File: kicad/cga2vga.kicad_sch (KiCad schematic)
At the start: 18 parts, among them J1 Conn_02x24_Counter_Clockwise, J2 CGA, J3 VGA, J4 5V, U1 MCP1700-3302E_TO92, U2 SN74LVC245A, U3 SN74LVC245A

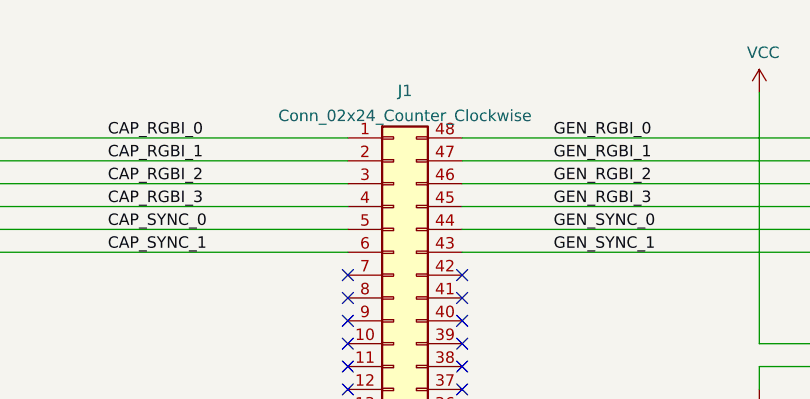
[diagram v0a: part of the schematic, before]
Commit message: Fix power connector marking
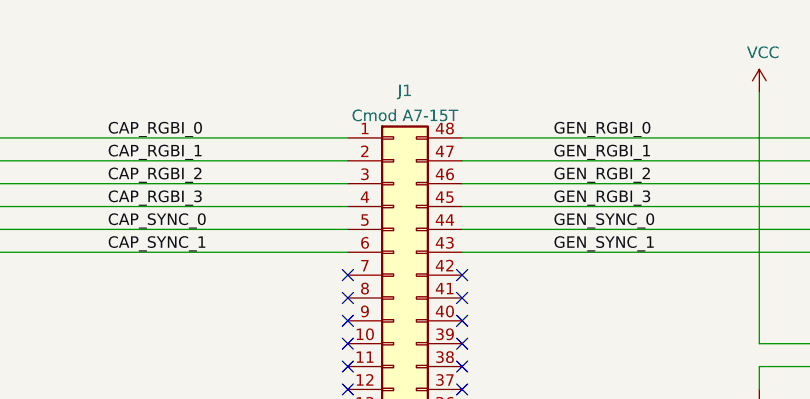
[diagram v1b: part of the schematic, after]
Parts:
- J1: value Conn_02x24_Counter_Clockwise -> Cmod A7-15T
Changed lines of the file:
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@@
     (in_bom yes) (on_board yes) (fields_autoplaced)
     (property "Reference" "J1" (id 0) (at 115.57 44.2935 0))
-    (property "Value" "Conn_02x24_Counter_Clockwise" (id 1) (at 115.57 47.0686 0))
+    (property "Value" "Cmod A7-15T" (id 1) (at 115.57 47.0686 0))
     (property "Footprint" "Package_DIP:DIP-48_W15.24mm_Socket" (id 2) (at 114.3 77.47 0)
       (effects (font (size 1.27 1.27)) hide)
@@
     )
     (path "/4b708762-d3c8-47bb-814c-3cc2597abb3e"
-      (reference "J1") (unit 1) (value "Conn_02x24_Counter_Clockwise") (footprint "Package_DIP:DIP-48_W15.24mm_Socket")
+      (reference "J1") (unit 1) (value "Cmod A7-15T") (footprint "Package_DIP:DIP-48_W15.24mm_Socket")
     )
     (path "/1cf519d2-be13-4b0e-872d-366d38fed7f6"

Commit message: Fix color
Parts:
- added R5, R6: 680, Resistor_THT:R_Axial_DIN0207_L6.3mm_D2.5mm_P7.62mm_Horizontal, symbol Device:R
- R4: value 470 -> 680
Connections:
- net GEN_SYNC_0: now also J1.42 (Pin_42), U3.8 (A6); no longer J1.44 (Pin_44), U3.6 (A4)
- net GEN_SYNC_1: now also J1.41 (Pin_41), U3.9 (A7); no longer J1.43 (Pin_43), U3.7 (A5)
- net VGA_HSYNC: now also U3.12 (B6); no longer U3.14 (B4)
- net VGA_VSYNC: now also U3.11 (B7); no longer U3.13 (B5)
- net at D1.2 (A), R4.2: no longer D2.2 (A), D3.2 (A)
- net GEN_RGBI_0 renamed GEN_RGB0_0
- net GEN_RGBI_1 renamed GEN_RGB0_1
- net GEN_RGBI_2 renamed GEN_RGB0_2
- net GEN_RGBI_3 renamed GEN_RGB1_0
- new net: D2.2 (A), R5.2
- new net: R5.1, U3.14 (B4)
- new net: D3.2 (A), R6.2
- new net: R6.1, U3.13 (B5)
- new net GEN_RGB1_1: J1.44 (Pin_44), U3.6 (A4)
- new net GEN_RGB1_2: J1.43 (Pin_43), U3.7 (A5)
- no-connect marks 48 -> 42
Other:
- moved on the sheet: D1, D2, D3, R1, R2, R3, R4

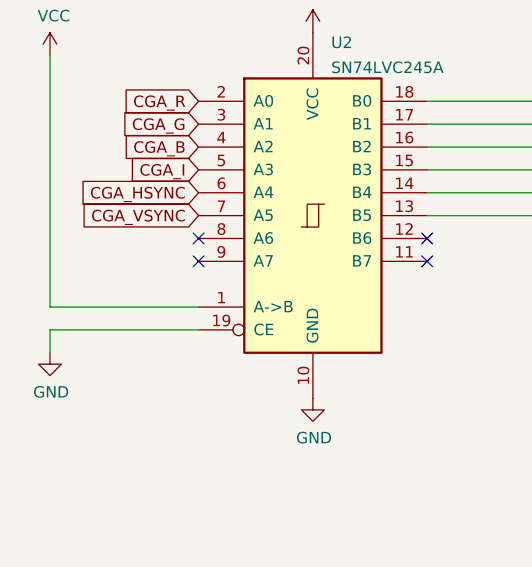
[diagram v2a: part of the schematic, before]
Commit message: Ground unused inputs
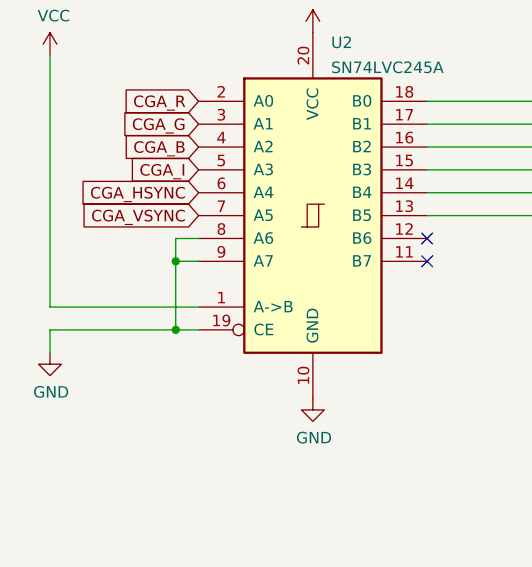
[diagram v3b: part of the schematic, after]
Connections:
- net GND: now also U2.8 (A6), U2.9 (A7)
- no-connect marks 42 -> 40
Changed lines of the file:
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@@
   (junction (at 243.84 57.15) (diameter 0) (color 0 0 0 0)
   )
+  (junction (at 40.64 67.31) (diameter 0) (color 0 0 0 0)
+  )
   (junction (at 86.36 189.23) (diameter 0) (color 0 0 0 0)
+  )
+  (junction (at 40.64 74.93) (diameter 0) (color 0 0 0 0)
   )
   (junction (at 73.66 181.61) (diameter 0) (color 0 0 0 0)
@@
   (no_connect (at 121.92 69.85))
   (no_connect (at 228.6 129.54))
-  (no_connect (at 43.18 64.77))
-  (no_connect (at 43.18 67.31))
   (no_connect (at 228.6 127))
   (no_connect (at 228.6 114.3))
@@
     (stroke (width 0) (type default) (color 0 0 0 0))
   )
+  (wire (pts (xy 40.64 64.77) (xy 40.64 67.31))
+    (stroke (width 0) (type default) (color 0 0 0 0))
+  )
+  (wire (pts (xy 40.64 74.93) (xy 43.18 74.93))
+    (stroke (width 0) (type default) (color 0 0 0 0))
+  )
   (wire (pts (xy 243.84 77.47) (xy 243.84 88.9))
     (stroke (width 0) (type default) (color 0 0 0 0))
@@
     (stroke (width 0) (type default) (color 0 0 0 0))
   )
+  (wire (pts (xy 40.64 67.31) (xy 43.18 67.31))
+    (stroke (width 0) (type default) (color 0 0 0 0))
+  )
   (wire (pts (xy 172.72 123.19) (xy 187.96 123.19))
     (stroke (width 0) (type default) (color 0 0 0 0))
@@
     (stroke (width 0) (type default) (color 0 0 0 0))
   )
+  (wire (pts (xy 40.64 67.31) (xy 40.64 74.93))
+    (stroke (width 0) (type default) (color 0 0 0 0))
+  )
   (wire (pts (xy 191.77 62.23) (xy 210.82 62.23))
     (stroke (width 0) (type default) (color 0 0 0 0))
@@
     (stroke (width 0) (type default) (color 0 0 0 0))
   )
-  (wire (pts (xy 26.67 74.93) (xy 43.18 74.93))
-    (stroke (width 0) (type default) (color 0 0 0 0))
-  )
+  (wire (pts (xy 43.18 64.77) (xy 40.64 64.77))
+    (stroke (width 0) (type default) (color 0 0 0 0))
+  )
+  (wire (pts (xy 26.67 74.93) (xy 40.64 74.93))
+    (stroke (width 0) (type default) (color 0 0 0 0))
+  )

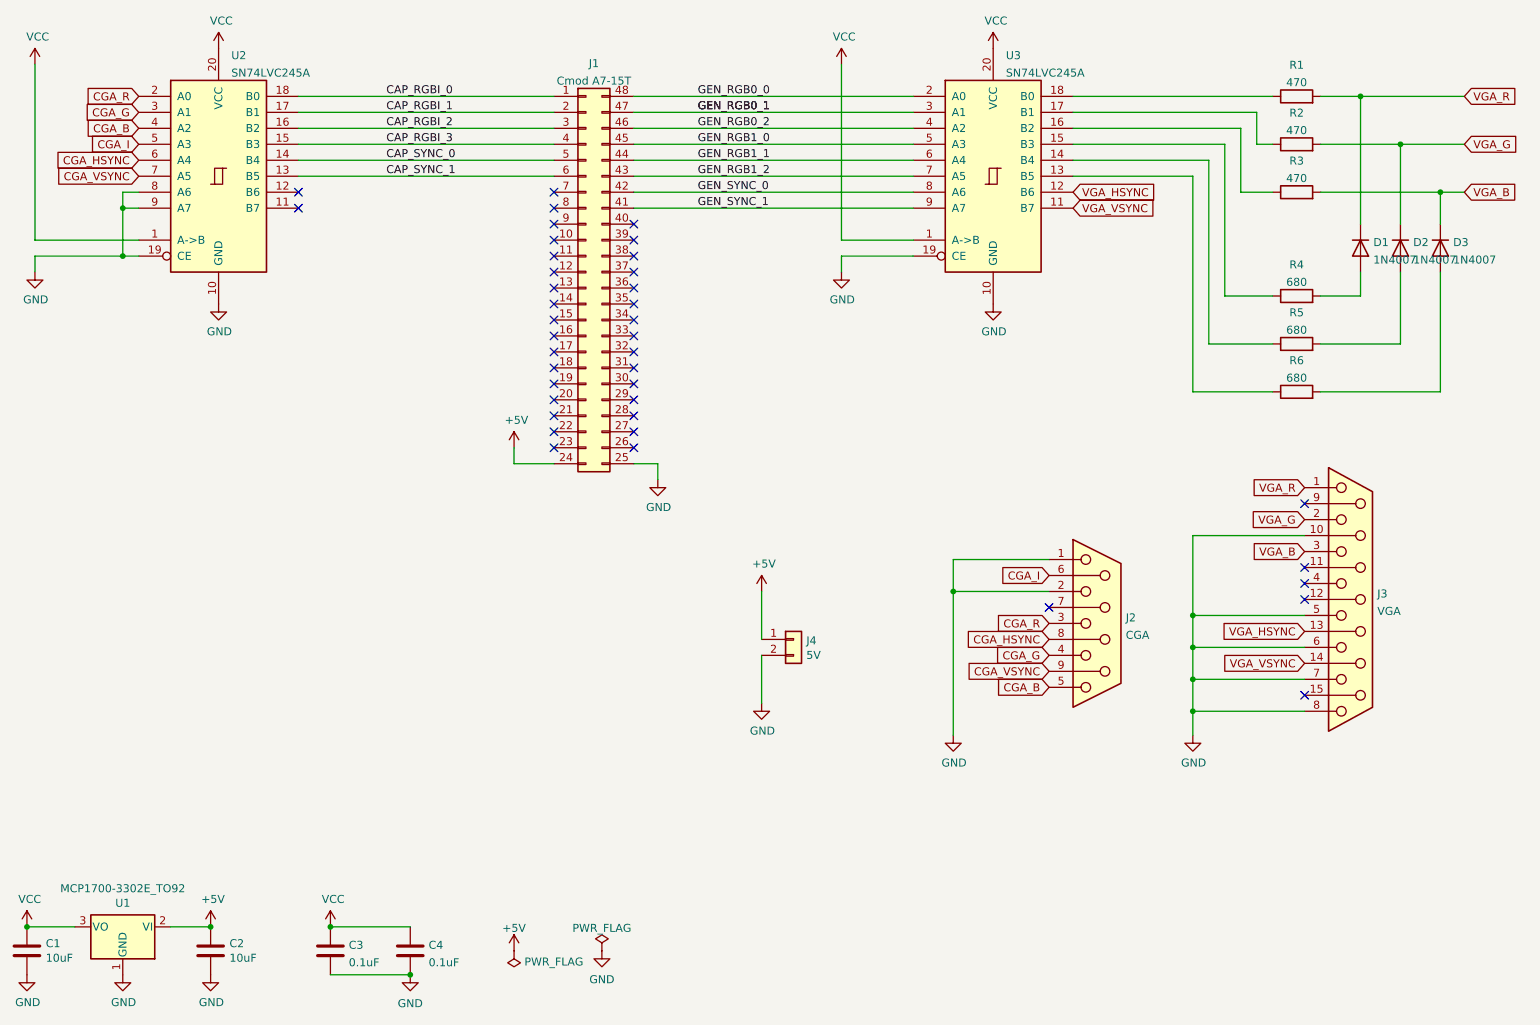
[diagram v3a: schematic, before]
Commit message: Update schematic to reflect CMOD pin names
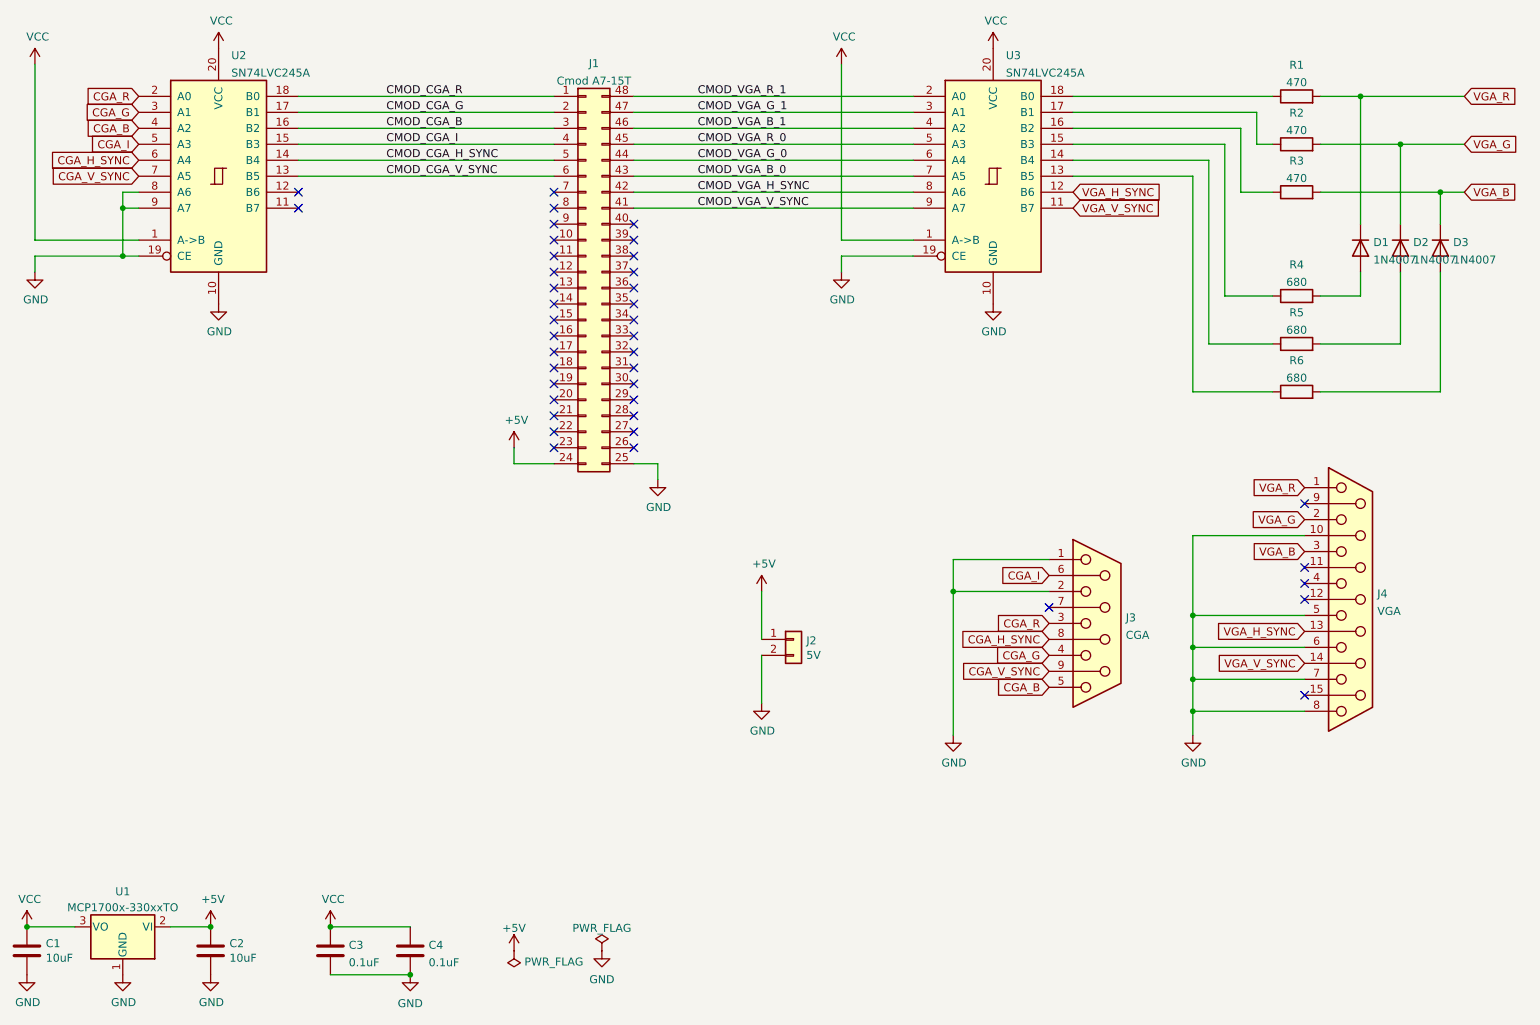
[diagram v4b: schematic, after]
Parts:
- removed U1: MCP1700-3302E_TO92, Package_TO_SOT_THT:TO-92_HandSolder, symbol Regulator_Linear:MCP1700-3302E_TO92
- added U1: MCP1700x-330xxTO, Package_TO_SOT_THT:TO-92_Inline, symbol Regulator_Linear:MCP1700x-330xxTO
- renumbered J4 to J2, J2 to J3, J3 to J4
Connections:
- net +5V: now also U1.2 (VI)
- net GND: now also U1.1 (GND)
- net VCC: now also U1.3 (VO)
- net CAP_RGBI_0 renamed CMOD_CGA_R
- net CAP_RGBI_1 renamed CMOD_CGA_G
- net CAP_RGBI_2 renamed CMOD_CGA_B
- net CAP_RGBI_3 renamed CMOD_CGA_I
- net CAP_SYNC_0 renamed CMOD_CGA_H_SYNC
- net CAP_SYNC_1 renamed CMOD_CGA_V_SYNC
- net CGA_HSYNC renamed CGA_H_SYNC
- net CGA_VSYNC renamed CGA_V_SYNC
- net GEN_RGB0_0 renamed CMOD_VGA_R_1
- net GEN_RGB0_1 renamed CMOD_VGA_G_1
- net GEN_RGB0_2 renamed CMOD_VGA_B_1
- net GEN_RGB1_0 renamed CMOD_VGA_R_0
- net GEN_RGB1_1 renamed CMOD_VGA_G_0
- net GEN_RGB1_2 renamed CMOD_VGA_B_0
- net GEN_SYNC_0 renamed CMOD_VGA_H_SYNC
- net GEN_SYNC_1 renamed CMOD_VGA_V_SYNC
- net VGA_HSYNC renamed VGA_H_SYNC
- net VGA_VSYNC renamed VGA_V_SYNC
